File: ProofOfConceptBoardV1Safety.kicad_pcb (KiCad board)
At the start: 2 copper layers, 42 parts, among them U1 MCP2515-EST, U2 MCP2515-EST

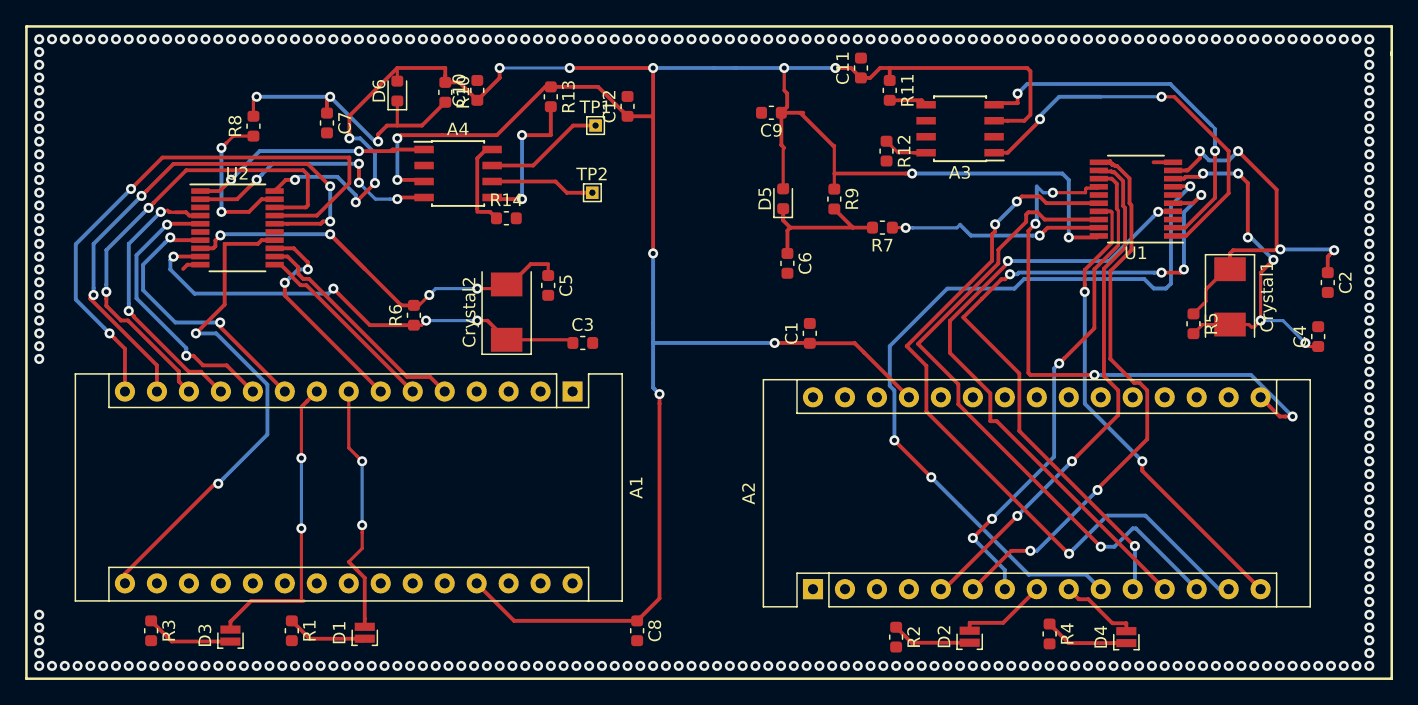
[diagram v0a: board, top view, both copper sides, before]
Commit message: 0.0.5 Changes to board after review. Also with og backup.  Sch changes
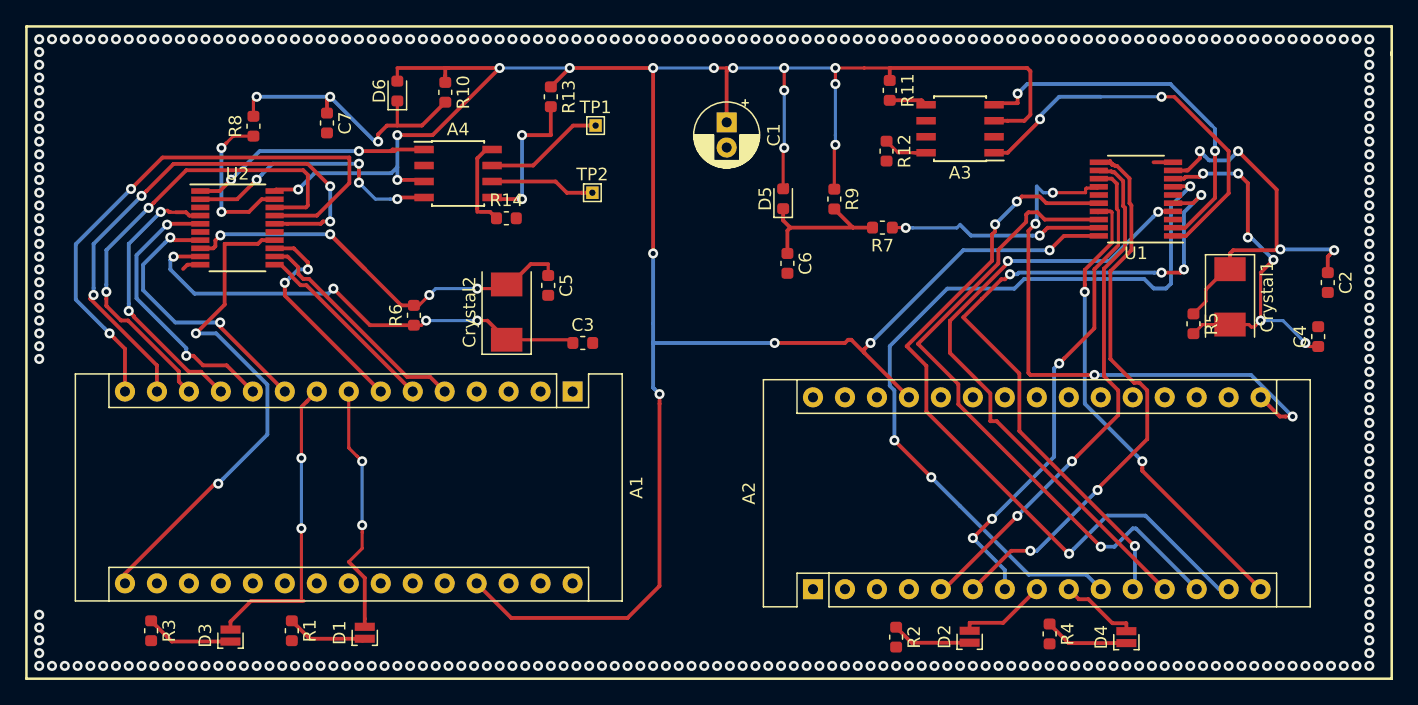
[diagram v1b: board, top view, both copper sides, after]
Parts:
- removed C10, C11, C12, C8, C9: 100nF, Capacitor_SMD:C_0603_1608Metric
- C1: value 100nF -> 100uF; footprint Capacitor_SMD:C_0603_1608Metric -> Capacitor_THT:CP_Radial_D5.0mm_P2.00mm
- moved C1 18.0 mm to (124.7, 64.3), turned to 270 degrees
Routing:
- net +5V: track 241.1 -> 216.8 mm, vias 16 -> 19
